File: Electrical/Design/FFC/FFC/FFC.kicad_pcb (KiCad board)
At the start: 2 copper layers, 13 x 15 mm, 4 parts, among them J1 Conn_01x08, J2 Conn_01x08

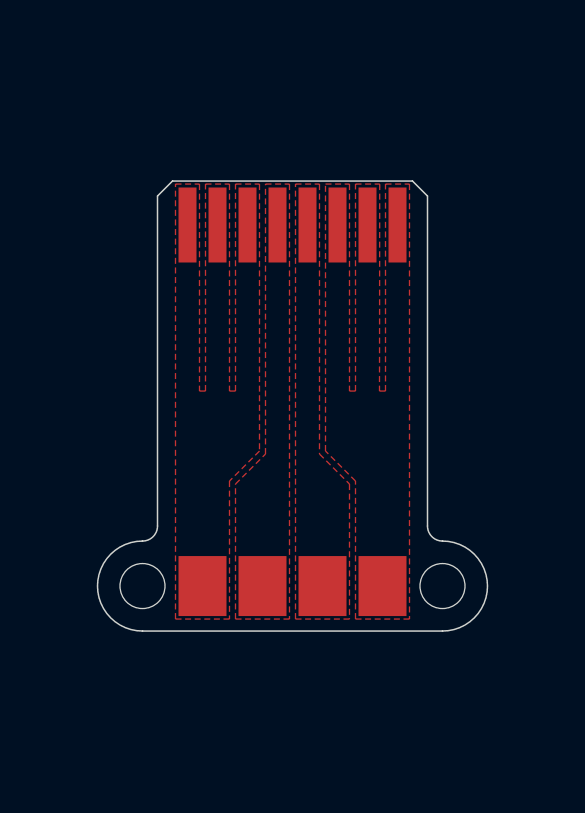
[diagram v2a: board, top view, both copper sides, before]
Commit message: SUKU interface & FFC iteration
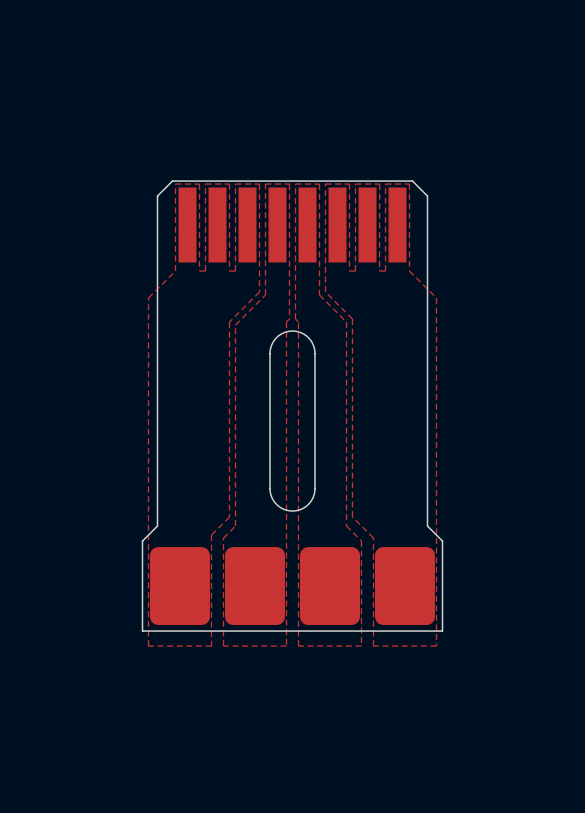
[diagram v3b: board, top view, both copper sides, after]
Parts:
- removed H1, H2: MountingHole, suku_basics:J_FFC_1.5mm_ALIGNMENT
- J2: footprint suku_basics:J_FFC_1x8_SOLDER_2 -> suku_basics:J_FFC_1x8_Solder_3common_SMT
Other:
- board size 13 x 15 mm -> 10 x 15 mm
- board text added: "20 7"
- board text removed: "2020/4"
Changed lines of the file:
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@@
-(kicad_pcb (version 20171130) (host pcbnew "(5.1.2)-2")
+(kicad_pcb (version 20171130) (host pcbnew "(5.1.6)-1")
   (general
     (thickness 0.1)
@@
     (tracks 0)
     (zones 0)
-    (modules 4)
+    (modules 2)
     (nets 5)
   )
@@
     (add_net "Net-(J1-Pad6)")
   )
-  (module suku_basics:J_FFC_1x8_SOLDER_2 (layer F.Cu)
+  (module suku_basics:J_FFC_1x8_Solder_3common_SMT (layer F.Cu)
     (at 100 98.5)
+    (descr "TE FPC connector, 08 bottom-side contacts, 1.0mm pitch, 1.0mm height, SMT, http://www.te.com/commerce/DocumentDelivery/DDEController?Action=srchrtrv&DocNm=84952&DocType=Customer+Drawing&DocLang=English&DocFormat=pdf&PartCntxt=84952-4")
+    (tags "te fpc 84952")
     (attr smd)
-    (fp_text reference J2 (at 0 4.5 180) (layer F.SilkS) hide
-      (effects (font (size 1 1) (thickness 0.15)))
-    )
-    (fp_text value Conn_01x08 (at 0 3 180) (layer F.Fab) hide
-      (effects (font (size 1 1) (thickness 0.15)))
-    )
-    (fp_text user %R (at 0 0 180) (layer F.Fab) hide
-      (effects (font (size 1 1) (thickness 0.15)))
-    )
-    (fp_line (start -4.5 -2.25) (end -4.5 2.25) (layer F.CrtYd) (width 0.05))
-    (fp_line (start 4.5 -2.25) (end -4.5 -2.25) (layer F.CrtYd) (width 0.05))
-    (fp_line (start 4.5 2.25) (end 4.5 -2.25) (layer F.CrtYd) (width 0.05))
-    (fp_line (start -4.5 2.25) (end 4.5 2.25) (layer F.CrtYd) (width 0.05))
-    (pad 8 smd rect (at 3 0 90) (size 2 1.6) (layers F.Cu F.Paste F.Mask)
-      (net 1 "Net-(J1-Pad6)"))
-    (pad 4 smd rect (at -1 0 90) (size 2 1.6) (layers F.Cu F.Paste F.Mask)
+    (fp_text reference J2 (at 0 2) (layer F.SilkS) hide
+      (effects (font (size 1 1) (thickness 0.15)))
+    )
+    (fp_text value Conn_01x08 (at 0 3) (layer F.Fab) hide
+      (effects (font (size 1 1) (thickness 0.15)))
+    )
+    (fp_text user %R (at 0 0) (layer B.Fab)
+      (effects (font (size 1 1) (thickness 0.15)) (justify mirror))
+    )
+    (fp_line (start -5 2) (end -5 -2) (layer B.CrtYd) (width 0.12))
+    (fp_line (start 5 2) (end -5 2) (layer B.CrtYd) (width 0.12))
+    (fp_line (start 5 -2) (end 5 2) (layer B.CrtYd) (width 0.12))
+    (fp_line (start -5 -2) (end 5 -2) (layer B.CrtYd) (width 0.12))
+    (pad 8 smd roundrect (at 3.75 0) (size 2 2.6) (layers F.Cu F.Paste F.Mask) (roundrect_rratio 0.139)
+      (net 1 "Net-(J1-Pad6)"))
+    (pad 5 smd roundrect (at 1.25 0) (size 2 2.6) (layers F.Cu F.Paste F.Mask) (roundrect_rratio 0.139)
+      (net 3 "Net-(J1-Pad5)"))
+    (pad 4 smd roundrect (at -1.25 0) (size 2 2.6) (layers F.Cu F.Paste F.Mask) (roundrect_rratio 0.139)
       (net 2 "Net-(J1-Pad4)"))
-    (pad 5 smd rect (at 1 0 90) (size 2 1.6) (layers F.Cu F.Paste F.Mask)
-      (net 3 "Net-(J1-Pad5)"))
-    (pad 1 smd rect (at -3 0 90) (size 2 1.6) (layers F.Cu F.Paste F.Mask)
+    (pad 1 smd roundrect (at -3.75 0) (size 2 2.6) (layers F.Cu F.Paste F.Mask) (roundrect_rratio 0.139)
       (net 4 "Net-(J1-Pad1)"))
   )
@@
       (effects (font (size 1 1) (thickness 0.15)))
     )
+    (fp_line (start -4.5 2.25) (end 4.5 2.25) (layer F.CrtYd) (width 0.05))
+    (fp_line (start 4.5 2.25) (end 4.5 -2.25) (layer F.CrtYd) (width 0.05))
+    (fp_line (start 4.5 -2.25) (end -4.5 -2.25) (layer F.CrtYd) (width 0.05))
     (fp_line (start -4.5 -2.25) (end -4.5 2.25) (layer F.CrtYd) (width 0.05))
-    (fp_line (start 4.5 -2.25) (end -4.5 -2.25) (layer F.CrtYd) (width 0.05))
-    (fp_line (start 4.5 2.25) (end 4.5 -2.25) (layer F.CrtYd) (width 0.05))
-    (fp_line (start -4.5 2.25) (end 4.5 2.25) (layer F.CrtYd) (width 0.05))
     (pad 8 smd rect (at 3.5 0 90) (size 2.5 0.6) (layers F.Cu F.Paste F.Mask)
       (net 1 "Net-(J1-Pad6)"))
@@
       (net 4 "Net-(J1-Pad1)"))
   )
-  (module suku_basics:J_FFC_1.5mm_ALIGNMENT (layer B.Cu)
-    (at 105 98.5)
-    (descr "Mounting Hole 2mm, no annular")
-    (tags "mounting hole 2mm no annular")
-    (attr virtual)
-    (fp_text reference H2 (at 1.5 2.5) (layer B.SilkS) hide
-      (effects (font (size 1 1) (thickness 0.15)) (justify mirror))
-    )
-    (fp_text value MountingHole (at 7.2 -0.1) (layer B.Fab) hide
-      (effects (font (size 1 1) (thickness 0.15)) (justify mirror))
-    )
-    (fp_line (start 0 -1) (end 0 -2) (layer B.SilkS) (width 0.12))
-    (fp_line (start -1 0) (end -2 0) (layer B.SilkS) (width 0.12))
-    (fp_line (start 0 1) (end 0 2) (layer B.SilkS) (width 0.12))
-    (fp_line (start 1 0) (end 2 0) (layer B.SilkS) (width 0.12))
-    (fp_text user %R (at 0.3 0) (layer B.Fab) hide
-      (effects (font (size 1 1) (thickness 0.15)) (justify mirror))
-    )
-    (pad "" np_thru_hole circle (at 0 0) (size 1.5 1.5) (drill 1.5) (layers *.Cu *.Mask))
-  )
-  (module suku_basics:J_FFC_1.5mm_ALIGNMENT (layer B.Cu)
-    (at 95 98.5)
-    (descr "Mounting Hole 2mm, no annular")
-    (tags "mounting hole 2mm no annular")
-    (attr virtual)
-    (fp_text reference H1 (at -1.5 2.5) (layer B.SilkS) hide
-      (effects (font (size 1 1) (thickness 0.15)) (justify mirror))
-    )
-    (fp_text value MountingHole (at -7.3 0.1) (layer B.Fab) hide
-      (effects (font (size 1 1) (thickness 0.15)) (justify mirror))
-    )
-    (fp_line (start 0 -1) (end 0 -2) (layer B.SilkS) (width 0.12))
-    (fp_line (start -1 0) (end -2 0) (layer B.SilkS) (width 0.12))
-    (fp_line (start 0 1) (end 0 2) (layer B.SilkS) (width 0.12))
-    (fp_line (start 1 0) (end 2 0) (layer B.SilkS) (width 0.12))
-    (fp_text user %R (at 0.3 0) (layer B.Fab) hide
-      (effects (font (size 1 1) (thickness 0.15)) (justify mirror))
-    )
-    (pad "" np_thru_hole circle (at 0 0) (size 1.5 1.5) (drill 1.5) (layers *.Cu *.Mask))
-  )
-  (gr_circle (center 97 95.5) (end 97.25 95.5) (layer F.Mask) (width 0.5))
-  (gr_circle (center 99 95.5) (end 99.25 95.5) (layer F.Mask) (width 0.5))
-  (gr_circle (center 101 95.5) (end 101.25 95.5) (layer F.Mask) (width 0.5))
-  (gr_circle (center 103 95.5) (end 103.25 95.5) (layer F.Mask) (width 0.5))
-  (gr_line (start 96.5 94.5) (end 96.5 92.5) (layer B.SilkS) (width 0.12))
-  (gr_line (start 103.5 94.5) (end 96.5 94.5) (layer B.SilkS) (width 0.12))
-  (gr_line (start 103.5 92.5) (end 103.5 94.5) (layer B.SilkS) (width 0.12))
-  (gr_line (start 96.5 92.5) (end 103.5 92.5) (layer B.SilkS) (width 0.12))
-  (gr_text 2020/4 (at 100 93.5) (layer B.SilkS)
+  (gr_line (start 96.25 94.75) (end 96.25 91.25) (layer B.SilkS) (width 0.12))
+  (gr_line (start 98.75 94.75) (end 96.25 94.75) (layer B.SilkS) (width 0.12))
+  (gr_line (start 98.75 91.25) (end 98.75 94.75) (layer B.SilkS) (width 0.12))
+  (gr_line (start 96.25 91.25) (end 98.75 91.25) (layer B.SilkS) (width 0.12))
+  (gr_line (start 100.75 95.25) (end 100.75 90.75) (layer Edge.Cuts) (width 0.05))
+  (gr_line (start 99.25 90.75) (end 99.25 95.25) (layer Edge.Cuts) (width 0.05))
+  (gr_arc (start 100 95.25) (end 99.25 95.25) (angle -180) (layer Edge.Cuts) (width 0.05))
+  (gr_arc (start 100 90.75) (end 100.75 90.75) (angle -180) (layer Edge.Cuts) (width 0.05))
+  (gr_line (start 105 97) (end 104.5 96.5) (layer Edge.Cuts) (width 0.05))
+  (gr_line (start 95 97) (end 95.5 96.5) (layer Edge.Cuts) (width 0.05))
+  (gr_line (start 95 100) (end 95 97) (layer Edge.Cuts) (width 0.05))
+  (gr_line (start 105 100) (end 105 97) (layer Edge.Cuts) (width 0.05))
+  (gr_text "20\n7" (at 97.5 93) (layer B.SilkS)
     (effects (font (size 1 1) (thickness 0.15)) (justify mirror))
   )
-  (gr_arc (start 95 96.5) (end 95 97) (angle -90) (layer Edge.Cuts) (width 0.05))
-  (gr_arc (start 105 96.5) (end 104.5 96.5) (angle -90) (layer Edge.Cuts) (width 0.05))
-  (gr_arc (start 105 98.5) (end 105 100) (angle -180) (layer Edge.Cuts) (width 0.05))
-  (gr_arc (start 95 98.5) (end 95 97) (angle -180) (layer Edge.Cuts) (width 0.05))
   (gr_text "PI STIFFENER\nTO FFC CONNECTOR" (at 94 87) (layer B.SilkS)
     (effects (font (size 1 1) (thickness 0.15)) (justify right))
@@
     (polygon
       (pts
-        (xy 98.1 85.1) (xy 98.9 85.1) (xy 98.9 94) (xy 97.9 95) (xy 97.9 99.6)
-        (xy 96.1 99.6) (xy 96.1 85.1) (xy 96.9 85.1) (xy 96.9 92) (xy 97.1 92)
-        (xy 97.1 85.1) (xy 97.9 85.1) (xy 97.9 92) (xy 98.1 92)
+        (xy 98.1 85.1) (xy 98.9 85.1) (xy 98.9 88.7) (xy 97.9 89.7) (xy 97.9 96.2)
+        (xy 97.3 96.8) (xy 97.3 100.5) (xy 95.2 100.5) (xy 95.2 88.9) (xy 96.1 88)
+        (xy 96.1 85.1) (xy 96.9 85.1) (xy 96.9 88) (xy 97.1 88) (xy 97.1 85.1)
+        (xy 97.9 85.1) (xy 97.9 88) (xy 98.1 88)
       )
     )
@@
     (polygon
       (pts
-        (xy 98.1 95.1) (xy 99.1 94.1) (xy 99.1 85.1) (xy 99.9 85.1) (xy 99.9 99.6)
-        (xy 98.1 99.6)
+        (xy 97.7 96.9) (xy 98.1 96.5) (xy 98.1 89.8) (xy 99.1 88.8) (xy 99.1 85.1)
+        (xy 99.9 85.1) (xy 99.9 89.6) (xy 99.8 89.7) (xy 99.8 100.5) (xy 97.7 100.5)
       )
     )
@@
     (polygon
       (pts
-        (xy 100.1 85.1) (xy 100.9 85.1) (xy 100.9 94.1) (xy 101.9 95.1) (xy 101.9 99.6)
-        (xy 100.1 99.6)
+        (xy 100.2 89.7) (xy 100.1 89.6) (xy 100.1 85.1) (xy 100.9 85.1) (xy 100.9 88.8)
+        (xy 101.8 89.7) (xy 101.8 96.5) (xy 102.3 97) (xy 102.3 100.5) (xy 100.2 100.5)
       )
     )
@@
     (polygon
       (pts
-        (xy 102.1 95) (xy 101.1 94) (xy 101.1 85.1) (xy 101.9 85.1) (xy 101.9 92)
-        (xy 102.1 92) (xy 102.1 85.1) (xy 102.90789 85.1) (xy 102.9 92) (xy 103.1 92)
-        (xy 103.1 85.1) (xy 103.9 85.1) (xy 103.9 99.6) (xy 102.1 99.6)
-      )
-    )
+        (xy 102.7 96.9) (xy 102 96.2) (xy 102 89.6) (xy 101.1 88.7) (xy 101.1 85.1)
+        (xy 101.9 85.1) (xy 101.9 88) (xy 102.1 88) (xy 102.1 85.1) (xy 102.90789 85.1)
+        (xy 102.9 88) (xy 103.1 88) (xy 103.1 85.1) (xy 103.9 85.1) (xy 103.9 88)
+        (xy 104.8 88.9) (xy 104.8 100.5) (xy 102.7 100.5)
+      )
+    )
